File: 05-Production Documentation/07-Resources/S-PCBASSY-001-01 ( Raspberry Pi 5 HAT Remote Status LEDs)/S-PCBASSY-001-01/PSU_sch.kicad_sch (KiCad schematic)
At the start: 6 parts, among them J1 GPIO, U1 CAT24C256

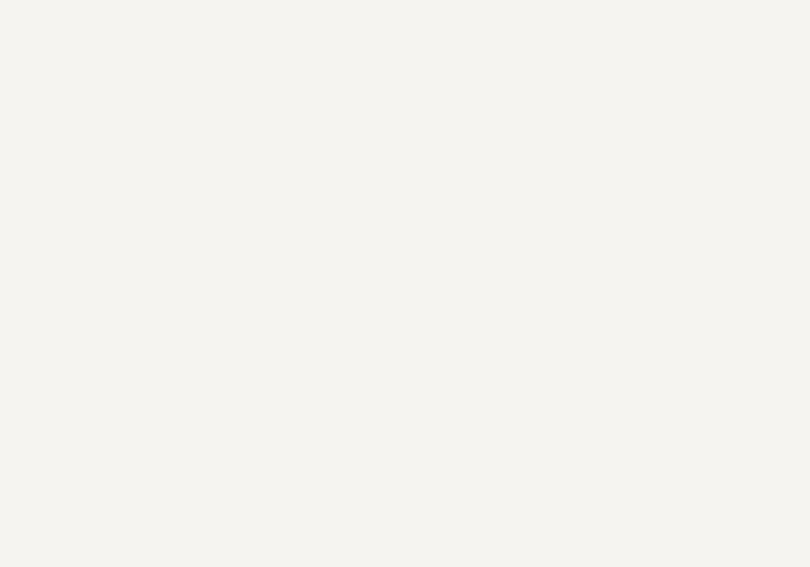
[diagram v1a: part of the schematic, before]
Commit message: Connector added with TVS still need to add polarity Protection
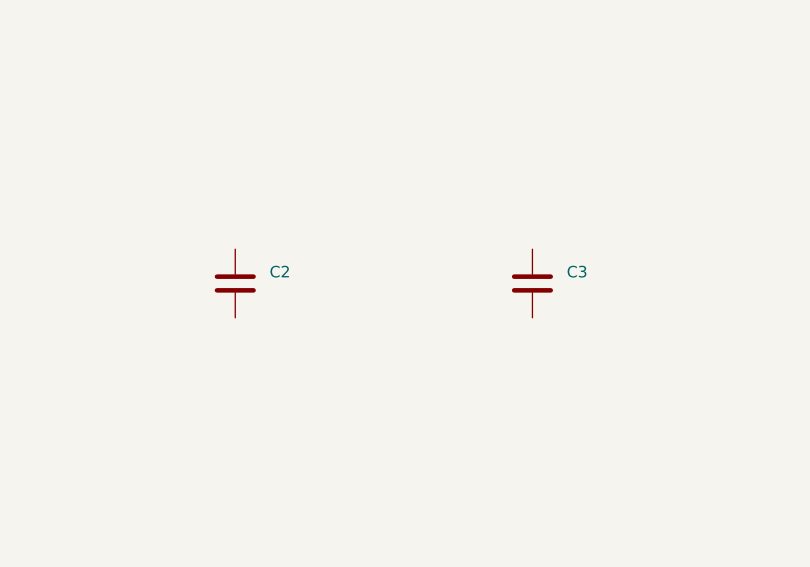
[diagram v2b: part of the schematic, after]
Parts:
- added C2: KEMET T491A106K016AT, Capacitor_Tantalum_SMD:CP_EIA-3216-18_Kemet-A, symbol Device:C
- added C3: Samsung CL21B104KBCNNNC, Capacitor_SMD:C_0805_2012Metric, symbol Device:C
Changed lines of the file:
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@@
+	)
+	(symbol
+		(lib_id "Device:C")
+		(at 181.61 58.42 0)
+		(unit 1)
+		(exclude_from_sim no)
+		(in_bom yes)
+		(on_board yes)
+		(dnp no)
+		(fields_autoplaced yes)
+		(property "Reference" "C3"
+			(at 185.42 57.1499 0)
+			(effects
+				(font
+					(size 1.27 1.27)
+				)
+				(justify left)
+			)
+		)
+		(property "Value" "Samsung CL21B104KBCNNNC"
+			(at 185.42 59.6899 0)
+			(effects
+				(font
+					(size 1.27 1.27)
+				)
+				(justify left)
+				(hide yes)
+			)
+		)
+		(property "Footprint" "Capacitor_SMD:C_0805_2012Metric"
+			(at 182.5752 62.23 0)
+			(effects
+				(font
+					(size 1.27 1.27)
+				)
+				(hide yes)
+			)
+		)
+		(property "Datasheet" "https://octopart.com/search?q=Samsung+CL21B104KBCNNNC&currency=USD&specs=0"
+			(at 181.61 58.42 0)
+			(effects
+				(font
+					(size 1.27 1.27)
+				)
+				(hide yes)
+			)
+		)
+		(property "Description" "Unpolarized capacitor"
+			(at 181.61 58.42 0)
+			(effects
+				(font
+					(size 1.27 1.27)
+				)
+				(hide yes)
+			)
+		)
+		(pin "2"
+		)
+		(pin "1"
+		)
+		(instances
+			(project "S-PCBASSY-001-01"
+				(path "/e63e39d7-6ac0-4ffd-8aa3-1841a4541b55/3b559bbf-d5c4-4e4e-8024-c1cb8f8bc431"
+					(reference "C3")
+					(unit 1)
+				)
+			)
+		)
 	)
 	(symbol
@@
 					(unit 1)
 				)
+			)
+		)
+	)
+	(symbol
+		(lib_id "Device:C")
+		(at 148.59 58.42 0)
+		(unit 1)
+		(exclude_from_sim no)
+		(in_bom yes)
+		(on_board yes)
+		(dnp no)
+		(fields_autoplaced yes)
+		(property "Reference" "C2"
+			(at 152.4 57.1499 0)
+			(effects
+				(font
+					(size 1.27 1.27)
+				)
+				(justify left)
+			)
+		)
+		(property "Value" "KEMET T491A106K016AT"
+			(at 152.4 59.6899 0)
+			(effects
+				(font
+					(size 1.27 1.27)
+				)
+				(justify left)
+				(hide yes)
+			)
+		)
+		(property "Footprint" "Capacitor_Tantalum_SMD:CP_EIA-3216-18_Kemet-A"
+			(at 149.5552 62.23 0)
+			(effects
+				(font
+					(size 1.27 1.27)
+				)
+				(hide yes)
+			)
+		)
+		(property "Datasheet" "https://octopart.com/part/kemet/T491A106K016AT"
+			(at 148.59 58.42 0)
+			(effects
+				(font
+					(size 1.27 1.27)
+				)
+				(hide yes)
+			)
+		)
+		(property "Description" "Unpolarized capacitor"
+			(at 148.59 58.42 0)
+			(effects
+				(font
+					(size 1.27 1.27)
+				)
+				(hide yes)
+			)
+		)
+		(pin "2"
+		)
+		(pin "1"
+		)
+		(instances
+			(project ""
+				(path "/e63e39d7-6ac0-4ffd-8aa3-1841a4541b55/3b559bbf-d5c4-4e4e-8024-c1cb8f8bc431"
+					(reference "C2")
+					(unit 1)
+				)

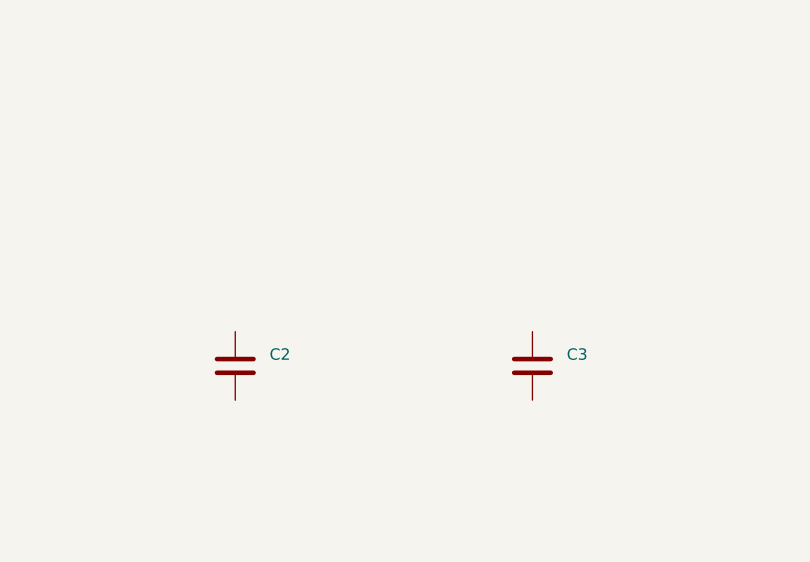
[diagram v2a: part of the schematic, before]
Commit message: Added Decolping caps
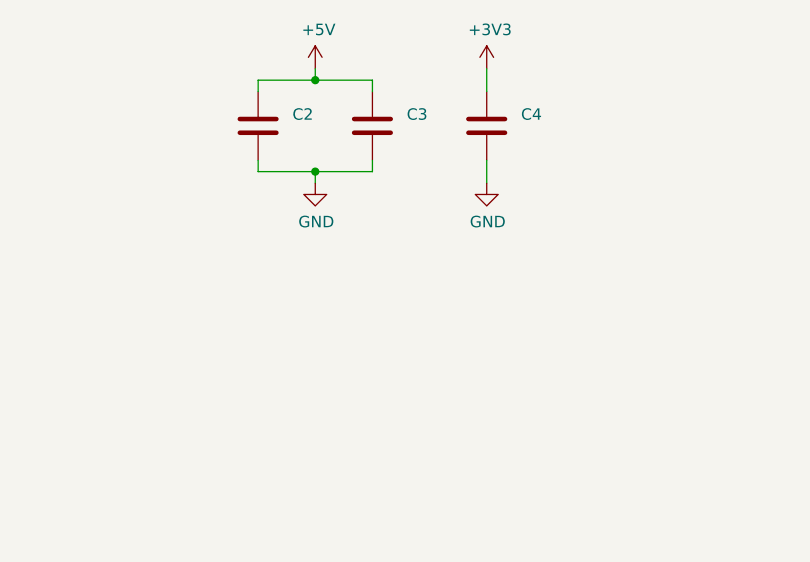
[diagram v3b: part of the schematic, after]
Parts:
- added C4: Samsung CL10B104KO8NNNC, Capacitor_SMD:C_0603_1608Metric, symbol Device:C
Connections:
- net +3V3: now also C4.1
- net +5V: now also C2.1, C3.1
- net GND: now also C2.2, C3.2, C4.2
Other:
- moved on the sheet: C2, C3

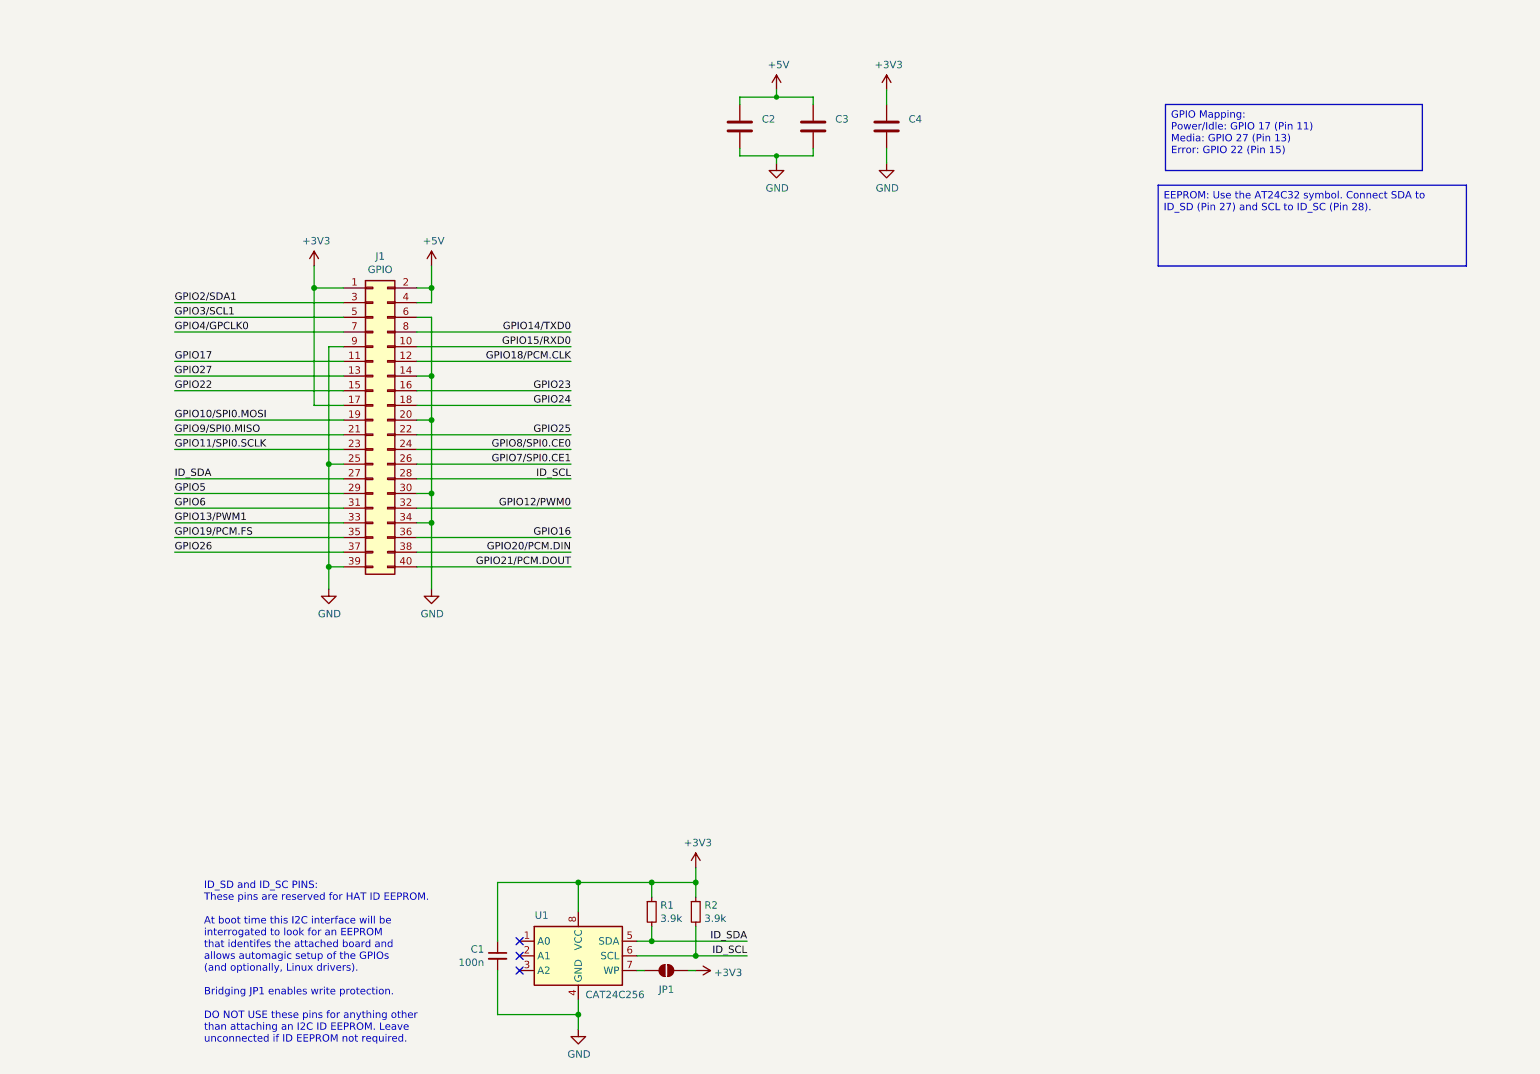
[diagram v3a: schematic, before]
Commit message: Rpi Filetring and protection added
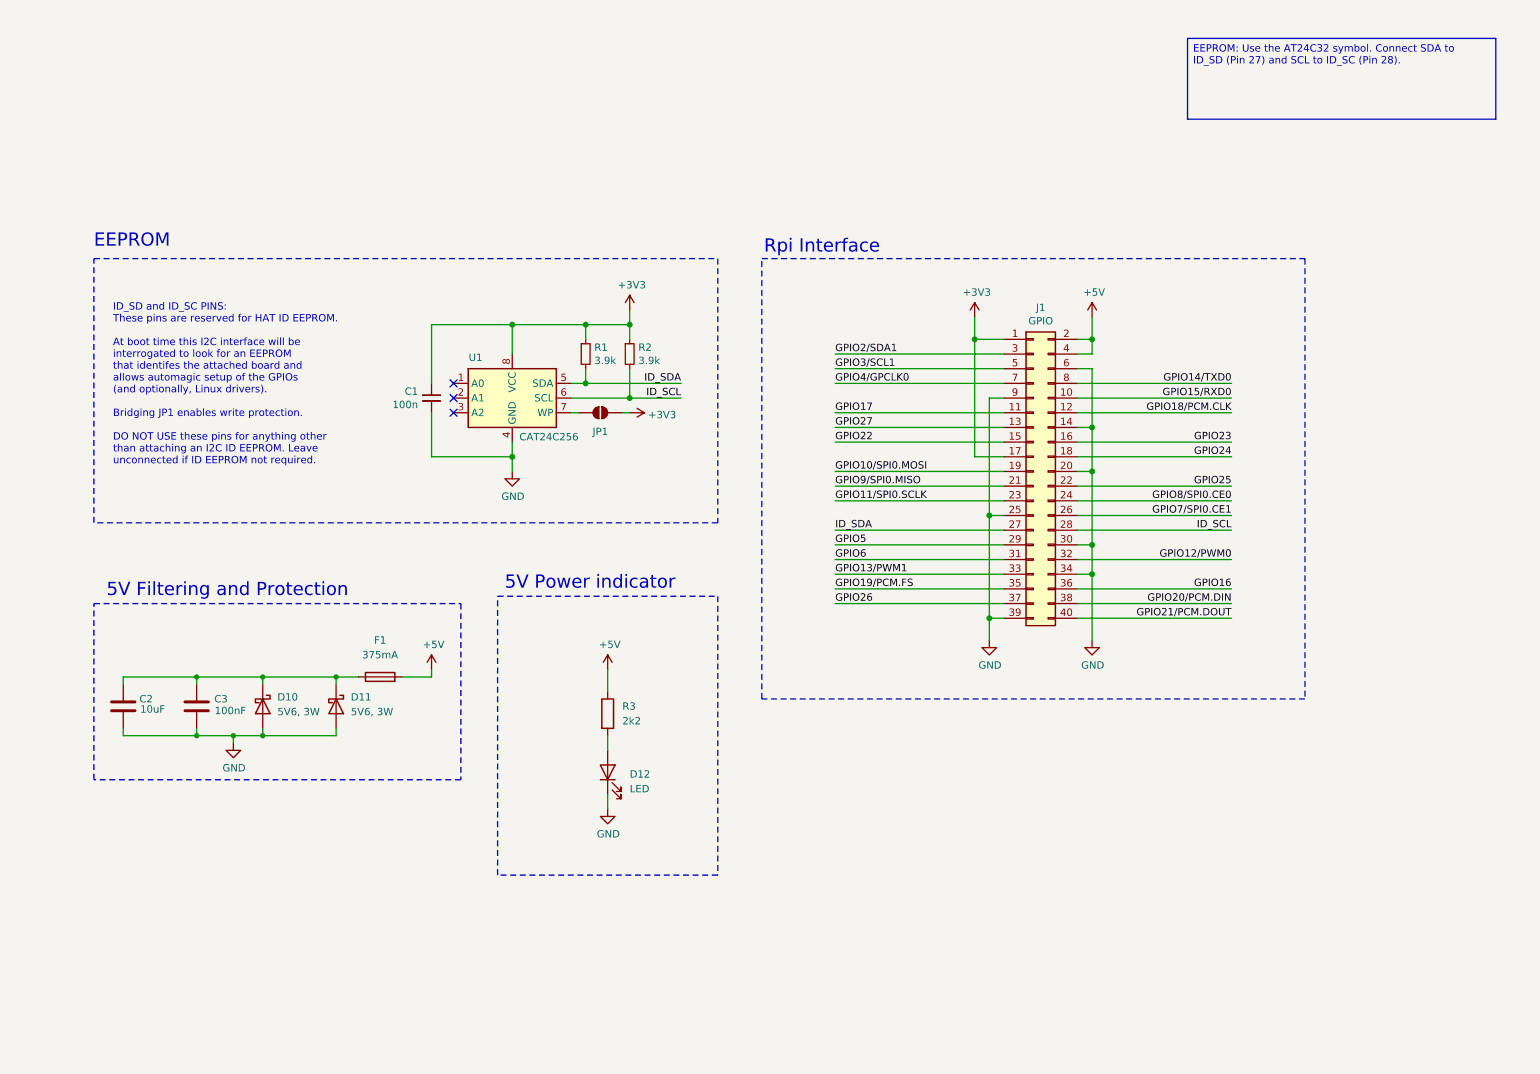
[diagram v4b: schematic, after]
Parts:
- removed C4: Samsung CL10B104KO8NNNC, Capacitor_SMD:C_0603_1608Metric, symbol Device:C
- added D10, D11: 5V6, 3W, Diode_SMD:D_SMA, symbol Diode:SS14
- added D12: LED, symbol Device:LED
- added F1: 375mA, Fuse:Fuse_0603_1608Metric, symbol Device:Fuse
- added R3: 2k2, Resistor_SMD:R_0603_1608Metric_Pad0.98x0.95mm_HandSolder, symbol Device:R
- C2: Cvalue (none) -> 10uF
- C3: Cvalue (none) -> 100nF
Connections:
- net +5V: now also F1.2, R3.1; no longer C2.1, C3.1
- net GND: now also D10.2 (A), D11.2 (A), D12.1 (K)
- new net: C2.1, C3.1, D10.1 (K), D11.1 (K), F1.1
- new net: D12.2 (A), R3.2
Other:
- note added: "5V Filtering and Protection"
- note added: "5V Power indicator"
- note added: "EEPROM"
- note added: "Rpi Interface"
- moved on the sheet: C1, C2, C3, J1, JP1, R1, R2, U1

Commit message: Schematics done
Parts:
- added D13: SS14, Diode_SMD:D_SMA, symbol Diode:SS14
- added Q4: AO3401A, Package_TO_SOT_SMD:SOT-23, symbol Transistor_FET:AO3401A
- added R4: 100k, Resistor_SMD:R_0603_1608Metric_Pad0.98x0.95mm_HandSolder, symbol Device:R
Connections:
- net +5V: now also D13.1 (K), Q4.2 (S); no longer F1.2
- net GND: now also R4.2
- net GPIO17 renamed POWER_LED_RPi
- net GPIO22 renamed ERROR_RPi
- net GPIO27 renamed MEDIA_LED_RPi
- new net: D13.2 (A), F1.2, Q4.3 (D)
- new net: Q4.1 (G), R4.1
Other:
- note added: "Notes"
- moved on the sheet: C2, C3, D10, D11, D12, F1, R3

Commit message: ERC Completed and passed
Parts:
- R1, R2: footprint (none) -> Capacitor_SMD:C_0603_1608Metric
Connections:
- no-connect marks 3 -> 26
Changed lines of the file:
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@@
+	)
+	(no_connect
+		(at 236.22 116.84)
+	)
+	(no_connect
+		(at 167.64 106.68)
+	)
+	(no_connect
+		(at 236.22 88.9)
+	)
+	(no_connect
+		(at 167.64 71.12)
+	)
+	(no_connect
+		(at 236.22 106.68)
+	)
+	(no_connect
+		(at 236.22 99.06)
 	)
 	(no_connect
@@
 	)
 	(no_connect
+		(at 167.64 76.2)
+	)
+	(no_connect
+		(at 236.22 86.36)
+	)
+	(no_connect
+		(at 236.22 81.28)
+	)
+	(no_connect
 		(at 101.6 81.28)
 	)
 	(no_connect
+		(at 167.64 91.44)
+	)
+	(no_connect
+		(at 167.64 111.76)
+	)
+	(no_connect
+		(at 236.22 114.3)
+	)
+	(no_connect
+		(at 236.22 111.76)
+	)
+	(no_connect
+		(at 167.64 109.22)
+	)
+	(no_connect
+		(at 167.64 104.14)
+	)
+	(no_connect
+		(at 167.64 96.52)
+	)
+	(no_connect
 		(at 101.6 78.74)
+	)
+	(no_connect
+		(at 236.22 76.2)
+	)
+	(no_connect
+		(at 236.22 78.74)
+	)
+	(no_connect
+		(at 236.22 93.98)
+	)
+	(no_connect
+		(at 167.64 114.3)
+	)
+	(no_connect
+		(at 167.64 93.98)
+	)
+	(no_connect
+		(at 167.64 73.66)
+	)
+	(no_connect
+		(at 236.22 96.52)
 	)
 	(wire
@@
 				(path "/e63e39d7-6ac0-4ffd-8aa3-1841a4541b55/3b559bbf-d5c4-4e4e-8024-c1cb8f8bc431"
 					(reference "#PWR04")
-					(unit 1)
-				)
-			)
-		)
-	)
-	(symbol
-		(lib_id "power:GND")
-		(at 212.09 120.65 0)
-		(unit 1)
-		(exclude_from_sim no)
-		(in_bom yes)
-		(on_board yes)
-		(dnp no)
-		(property "Reference" "#PWR02"
-			(at 212.09 127 0)
-			(effects
-				(font
-					(size 1.27 1.27)
-				)
-				(hide yes)
-			)
-		)
-		(property "Value" "GND"
-			(at 212.2043 124.9744 0)
-			(effects
-				(font
-					(size 1.27 1.27)
-				)
-			)
-		)
-		(property "Footprint" ""
-			(at 212.09 120.65 0)
-			(effects
-				(font
-					(size 1.27 1.27)
-				)
-			)
-		)
-		(property "Datasheet" ""
-			(at 212.09 120.65 0)
-			(effects
-				(font
-					(size 1.27 1.27)
-				)
-			)
-		)
-		(property "Description" "Power symbol creates a global label with name \"GND\" , ground"
-			(at 212.09 120.65 0)
-			(effects
-				(font
-					(size 1.27 1.27)
-				)
-				(hide yes)
-			)
-		)
-		(pin "1"
-		)
-		(instances
-			(project "S-PCBASSY-001-01"
-				(path "/e63e39d7-6ac0-4ffd-8aa3-1841a4541b55/3b559bbf-d5c4-4e4e-8024-c1cb8f8bc431"
-					(reference "#PWR02")
 					(unit 1)
 				)
@@
 			)
 		)
-		(property "Footprint" ""
+		(property "Footprint" "Capacitor_SMD:C_0603_1608Metric"
 			(at 124.46 71.12 0)
 			(effects
@@
 			)
 		)
-		(property "Footprint" ""
+		(property "Footprint" "Capacitor_SMD:C_0603_1608Metric"
 			(at 132.08 71.12 0)
 			(effects
@@
 					(unit 1)
 				)
+			)
+		)
+	)
+	(symbol
+		(lib_id "power:GND")
+		(at 212.09 120.65 0)
+		(unit 1)
+		(exclude_from_sim no)
+		(in_bom yes)
+		(on_board yes)
+		(dnp no)
+		(property "Reference" "#PWR02"
+			(at 212.09 127 0)
+			(effects
+				(font
+					(size 1.27 1.27)
+				)
+				(hide yes)
+			)
+		)
+		(property "Value" "GND"
+			(at 212.2043 124.9744 0)
+			(effects
+				(font
+					(size 1.27 1.27)
+				)
+			)
+		)
+		(property "Footprint" ""
+			(at 212.09 120.65 0)
+			(effects
+				(font
+					(size 1.27 1.27)
+				)
+			)
+		)
+		(property "Datasheet" ""
+			(at 212.09 120.65 0)
+			(effects
+				(font
+					(size 1.27 1.27)
+				)
+			)
+		)
+		(property "Description" "Power symbol creates a global label with name \"GND\" , ground"
+			(at 212.09 120.65 0)
+			(effects
+				(font
+					(size 1.27 1.27)
+				)
+				(hide yes)
+			)
+		)
+		(pin "1"
+		)
+		(instances
+			(project "S-PCBASSY-001-01"
+				(path "/e63e39d7-6ac0-4ffd-8aa3-1841a4541b55/3b559bbf-d5c4-4e4e-8024-c1cb8f8bc431"
+					(reference "#PWR02")
+					(unit 1)
+				)

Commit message: Imported Components to PCB
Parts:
- C1: footprint (none) -> Capacitor_SMD:C_0603_1608Metric
- D12: footprint (none) -> LED_SMD:LED_0603_1608Metric
- JP1: footprint (none) -> Connector_PinHeader_2.54mm:PinHeader_1x02_P2.54mm_Vertical_SMD_Pin1Left
- U1: footprint (none) -> Package_SO:SOIC-8_3.9x4.9mm_P1.27mm
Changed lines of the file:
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@@
 			)
 		)
-		(property "Footprint" ""
+		(property "Footprint" "Capacitor_SMD:C_0603_1608Metric"
 			(at 97.79 78.74 0)
 			(effects
@@
 			)
 		)
-		(property "Footprint" ""
+		(property "Footprint" "Connector_PinHeader_2.54mm:PinHeader_1x02_P2.54mm_Vertical_SMD_Pin1Left"
 			(at 127 81.28 0)
 			(effects
@@
 			)
 		)
-		(property "Footprint" ""
+		(property "Footprint" "Package_SO:SOIC-8_3.9x4.9mm_P1.27mm"
 			(at 111.76 78.74 0)
 			(effects
@@
 			)
 		)
-		(property "Footprint" ""
+		(property "Footprint" "LED_SMD:LED_0603_1608Metric"
 			(at 132.08 142.24 0)
 			(effects

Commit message: Layout done
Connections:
- net +5V: now also C2.1, C3.1, D10.1 (K), D11.1 (K), F1.1
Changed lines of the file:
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@@
+	)
+	(junction
+		(at 35.56 127)
+		(diameter 0)
+		(color 0 0 0 0)
 	)
 	(junction
@@
 			(width 0)
 			(type solid)
+		)
+	)
+	(wire
+		(pts
+			(xy 35.56 121.92) (xy 35.56 127)
+		)
+		(stroke
+			(width 0)
+			(type default)
 		)
 	)
@@
 					(unit 1)
 				)
+			)
+		)
+	)
+	(symbol
+		(lib_id "power:+5V")
+		(at 35.56 121.92 0)
+		(unit 1)
+		(exclude_from_sim no)
+		(in_bom yes)
+		(on_board yes)
+		(dnp no)
+		(property "Reference" "#PWR012"
+			(at 35.56 125.73 0)
+			(effects
+				(font
+					(size 1.27 1.27)
+				)
+				(hide yes)
+			)
+		)
+		(property "Value" "+5V"
+			(at 35.9283 117.5956 0)
+			(effects
+				(font
+					(size 1.27 1.27)
+				)
+			)
+		)
+		(property "Footprint" ""
+			(at 35.56 121.92 0)
+			(effects
+				(font
+					(size 1.27 1.27)
+				)
+			)
+		)
+		(property "Datasheet" ""
+			(at 35.56 121.92 0)
+			(effects
+				(font
+					(size 1.27 1.27)
+				)
+			)
+		)
+		(property "Description" "Power symbol creates a global label with name \"+5V\""
+			(at 35.56 121.92 0)
+			(effects
+				(font
+					(size 1.27 1.27)
+				)
+				(hide yes)
+			)
+		)
+		(pin "1"
+		)
+		(instances
+			(project "S-PCBASSY-001-01"
+				(path "/e63e39d7-6ac0-4ffd-8aa3-1841a4541b55/3b559bbf-d5c4-4e4e-8024-c1cb8f8bc431"
+					(reference "#PWR012")
+					(unit 1)
+				)
